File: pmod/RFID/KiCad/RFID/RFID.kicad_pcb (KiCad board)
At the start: 2 copper layers, 52.1 x 15.2 mm, 5 parts, among them J1 SPI IN, J3 SPI OUT

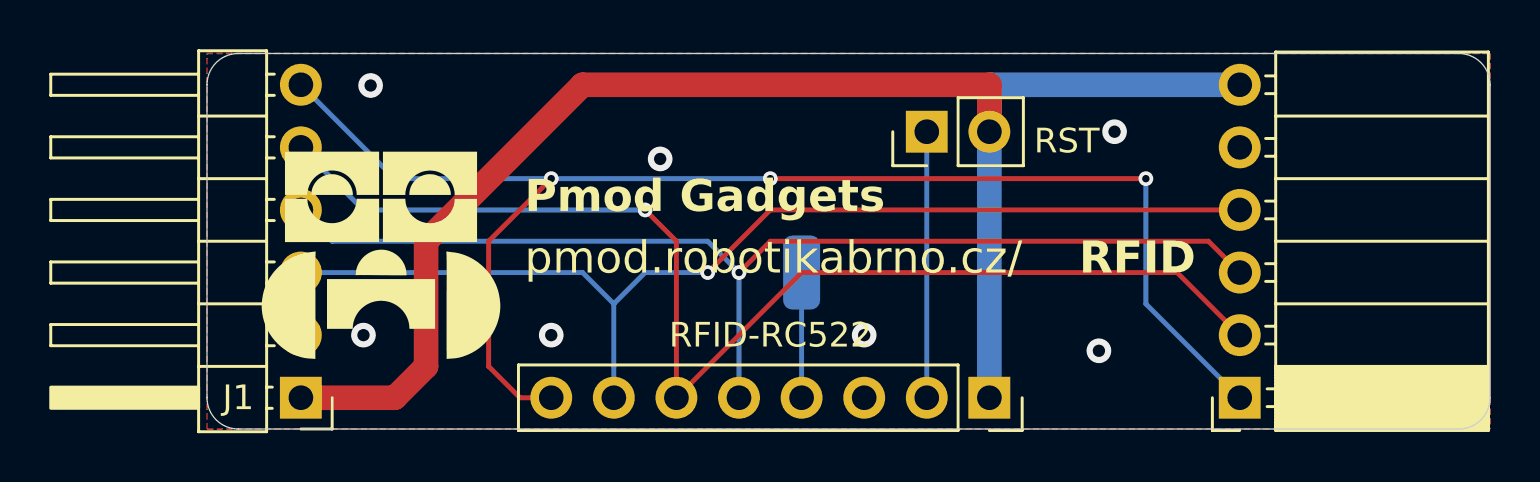
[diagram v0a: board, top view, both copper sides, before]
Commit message: Shrunk logos to not interfere with pins
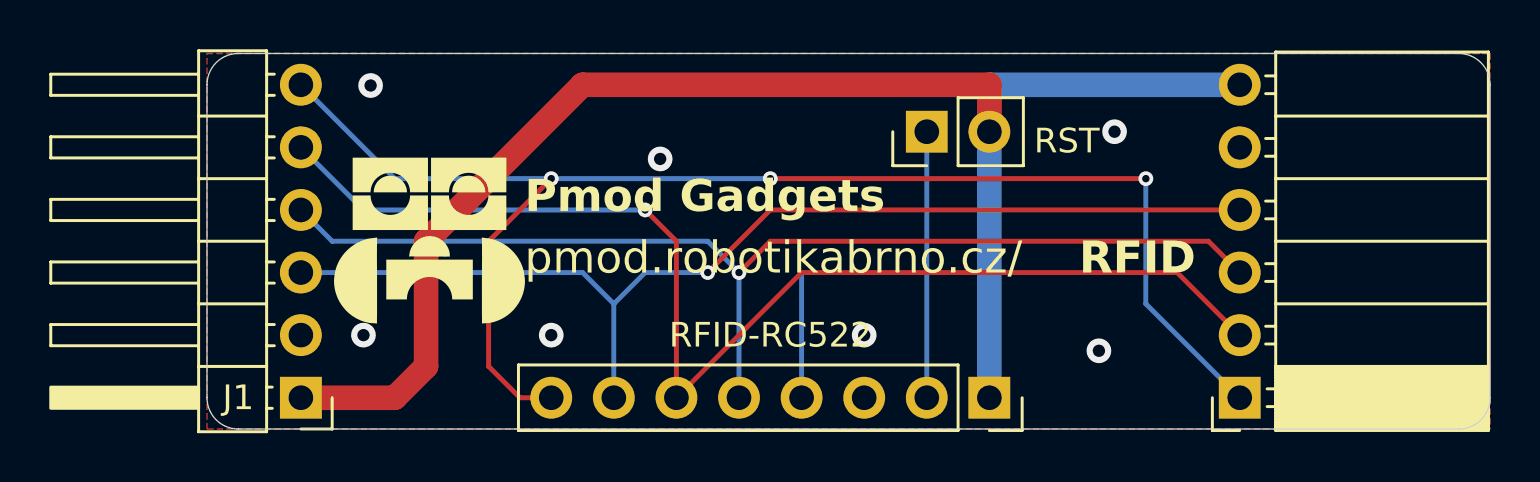
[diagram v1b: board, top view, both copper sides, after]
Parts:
- removed TP1: 1KQ, Connector_Wire:SolderWirePad_1x01_SMD_1.5x3mm

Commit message: minor fixes
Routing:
- net SS: track 58.1 -> 55.2 mm
- net GND: vias 7 -> 8
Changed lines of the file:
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@@
 			(psa4output no)
 			(plot_black_and_white yes)
+			(plotinvisibletext no)
 			(sketchpadsonfab no)
 			(plotpadnumbers no)
@@
 	)
 	(via
+		(at 65 58)
+		(size 0.6)
+		(drill 0.3)
+		(layers "F.Cu" "B.Cu")
+		(free yes)
+		(net 1)
+	)
+	(via
 		(at 91.44 47.625)
 		(size 1)
@@
 	)
 	(via
-		(at 68.58 55.88)
+		(at 70.2 55.88)
 		(size 1)
 		(drill 0.5)
@@
 	)
 	(via
-		(at 73 48.73)
+		(at 73.4 48)
 		(size 1)
 		(drill 0.5)
@@
 	)
 	(segment
-		(start 68.58 58.42)
-		(end 67.31 58.42)
-		(width 0.2)
-		(layer "F.Cu")
-		(net 5)
-	)
-	(segment
-		(start 67.31 58.42)
-		(end 66.04 57.15)
-		(width 0.2)
-		(layer "F.Cu")
-		(net 5)
-	)
-	(segment
-		(start 66.04 57.15)
-		(end 66.04 52.07)
-		(width 0.2)
-		(layer "F.Cu")
-		(net 5)
-	)
-	(segment
-		(start 66.04 52.07)
-		(end 68.58 49.53)
+		(start 68.58 49.53)
+		(end 68.58 58.42)
 		(width 0.2)
 		(layer "F.Cu")
@@
 		(priority 1)
 		(connect_pads
-			(clearance 0.5)
+			(clearance 0.25)
 		)
 		(min_thickness 0.25)
 		(filled_areas_thickness no)
 		(fill yes
-			(thermal_gap 0.5)
+			(thermal_gap 0.25)
 			(thermal_bridge_width 0.5)
 		)
@@
 		(hatch edge 0.5)
 		(connect_pads
-			(clearance 0.5)
+			(clearance 0.25)
 		)
 		(min_thickness 0.25)
 		(filled_areas_thickness no)
 		(fill yes
-			(thermal_gap 0.5)
+			(thermal_gap 0.25)
 			(thermal_bridge_width 0.5)
 		)

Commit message: fix: small pcb fixes
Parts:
- moved RFID-RC522 0.13 mm to (86.4, 58.3)
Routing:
- net Net-(J2-Pin_4): track 5.08 -> 0.00 mm
- net RST: track 11.4 -> 10.8 mm
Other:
- board size 52.1 x 15.2 mm -> 52.1 x 15.5 mm
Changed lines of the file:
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@@
 			(psa4output no)
 			(plot_black_and_white yes)
-			(plotinvisibletext no)
 			(sketchpadsonfab no)
 			(plotpadnumbers no)
@@
 	(footprint "Connector_PinSocket_2.54mm:PinSocket_1x08_P2.54mm_Vertical"
 		(layer "F.Cu")
-		(at 86.36 58.42 -90)
+		(at 86.36 58.293 -90)
 		(descr "Through hole straight socket strip, 1x08, 2.54mm pitch, single row (from Kicad 4.0.7), script generated")
 		(tags "Through hole socket strip THT 1x08 2.54mm single row")
@@
 	)
 	(gr_arc
-		(start 106.68 58.42)
-		(mid 106.308026 59.318026)
-		(end 105.41 59.69)
+		(start 106.68 58.547)
+		(mid 106.308026 59.445026)
+		(end 105.41 59.817)
 		(stroke
 			(width 0.05)
@@
 	)
 	(gr_line
-		(start 54.61 45.72)
-		(end 54.61 58.42)
+		(start 54.61 45.593)
+		(end 54.61 58.547)
 		(stroke
 			(width 0.05)
@@
 	)
 	(gr_arc
-		(start 54.61 45.72)
-		(mid 54.981974 44.821974)
-		(end 55.88 44.45)
+		(start 54.61 45.593)
+		(mid 54.981974 44.694974)
+		(end 55.88 44.323)
 		(stroke
 			(width 0.05)
@@
 	)
 	(gr_line
-		(start 106.68 58.42)
-		(end 106.68 45.72)
+		(start 106.68 58.547)
+		(end 106.68 45.593)
 		(stroke
 			(width 0.05)
@@
 	)
 	(gr_line
-		(start 55.88 59.69)
-		(end 105.41 59.69)
+		(start 55.88 59.817)
+		(end 105.41 59.817)
 		(stroke
 			(width 0.05)
@@
 	)
 	(gr_arc
-		(start 55.88 59.69)
-		(mid 54.981974 59.318026)
-		(end 54.61 58.42)
+		(start 55.88 59.817)
+		(mid 54.981974 59.445026)
+		(end 54.61 58.547)
 		(stroke
 			(width 0.05)
@@
 	)
 	(gr_arc
-		(start 105.41 44.45)
-		(mid 106.308026 44.821974)
-		(end 106.68 45.72)
+		(start 105.41 44.323)
+		(mid 106.308026 44.694974)
+		(end 106.68 45.593)
 		(stroke
 			(width 0.05)
@@
 	)
 	(gr_line
-		(start 105.41 44.45)
-		(end 55.88 44.45)
+		(start 105.41 44.323)
+		(end 55.88 44.323)
 		(stroke
 			(width 0.05)
@@
 		(start 95.25 52.07)
 		(end 77.47 52.07)
-		(width 0.2)
+		(width 0.3)
 		(layer "F.Cu")
 		(net 3)
@@
 		(start 77.47 52.07)
 		(end 76.2 53.34)
-		(width 0.2)
+		(width 0.3)
 		(layer "F.Cu")
 		(net 3)
@@
 		(start 96.52 53.34)
 		(end 95.25 52.07)
-		(width 0.2)
+		(width 0.3)
 		(layer "F.Cu")
 		(net 3)
@@
 		(start 74.93 52.07)
 		(end 76.2 53.34)
-		(width 0.2)
+		(width 0.3)
 		(layer "B.Cu")
 		(net 3)
@@
 		(start 58.42 50.8)
 		(end 59.69 52.07)
-		(width 0.2)
+		(width 0.3)
 		(layer "B.Cu")
 		(net 3)
@@
 		(start 59.69 52.07)
 		(end 74.93 52.07)
-		(width 0.2)
+		(width 0.3)
 		(layer "B.Cu")
 		(net 3)
@@
 		(start 76.2 53.34)
 		(end 76.2 58.42)
-		(width 0.2)
+		(width 0.3)
 		(layer "B.Cu")
 		(net 3)
@@
 		(start 77.47 50.8)
 		(end 96.52 50.8)
-		(width 0.2)
+		(width 0.3)
 		(layer "F.Cu")
 		(net 4)
@@
 		(start 74.93 53.34)
 		(end 77.47 50.8)
-		(width 0.2)
+		(width 0.3)
 		(layer "F.Cu")
 		(net 4)
@@
 		(start 74.93 53.34)
 		(end 72.39 53.34)
-		(width 0.2)
-		(layer "B.Cu")
-		(net 4)
-	)
-	(segment
-		(start 72.39 53.34)
-		(end 71.12 54.61)
-		(width 0.2)
+		(width 0.3)
 		(layer "B.Cu")
 		(net 4)
@@
 	(segment
 		(start 71.12 54.61)
-		(end 71.12 57.15)
-		(width 0.2)
+		(end 71.12 58.293)
+		(width 0.3)
 		(layer "B.Cu")
 		(net 4)
 	)
 	(segment
-		(start 71.12 57.15)
-		(end 71.12 58.42)
-		(width 0.2)
+		(start 72.39 53.34)
+		(end 71.12 54.61)
+		(width 0.3)
 		(layer "B.Cu")
 		(net 4)
@@
 		(start 69.85 53.34)
 		(end 71.12 54.61)
-		(width 0.2)
+		(width 0.3)
 		(layer "B.Cu")
 		(net 4)
@@
 		(start 58.42 53.34)
 		(end 69.85 53.34)
-		(width 0.2)
+		(width 0.3)
 		(layer "B.Cu")
 		(net 4)
@@
 		(start 68.58 49.53)
 		(end 68.58 58.42)
-		(width 0.2)
+		(width 0.3)
 		(layer "F.Cu")
 		(net 5)
@@
 		(start 77.47 49.53)
 		(end 92.71 49.53)
-		(width 0.2)
+		(width 0.3)
 		(layer "F.Cu")
 		(net 5)
@@
 		(start 68.58 49.53)
 		(end 77.47 49.53)
-		(width 0.2)
+		(width 0.3)
 		(layer "B.Cu")
 		(net 5)
@@
 		(start 68.58 49.53)
 		(end 62.23 49.53)
-		(width 0.2)
+		(width 0.3)
 		(layer "B.Cu")
 		(net 5)
@@
 		(start 92.71 54.61)
 		(end 96.52 58.42)
-		(width 0.2)
+		(width 0.3)
 		(layer "B.Cu")
 		(net 5)
@@
 		(start 92.71 49.53)
 		(end 92.71 54.61)
-		(width 0.2)
+		(width 0.3)
 		(layer "B.Cu")
 		(net 5)
@@
 		(start 62.23 49.53)
 		(end 58.42 45.72)
-		(width 0.2)
+		(width 0.3)
 		(layer "B.Cu")
 		(net 5)
 	)
 	(segment
-		(start 78.74 58.42)
-		(end 78.74 53.34)
-		(width 0.2)
-		(layer "B.Cu")
-		(net 6)
-	)
-	(segment
 		(start 83.82 58.42)
-		(end 83.82 46.99)
-		(width 0.2)
+		(end 83.82 47.625)
+		(width 0.3)
 		(layer "B.Cu")
 		(net 7)
@@
 		(start 72.39 50.8)
 		(end 73.66 52.07)
-		(width 0.2)
+		(width 0.3)
 		(layer "F.Cu")
 		(net 8)
@@
 		(start 78.74 53.34)
 		(end 93.98 53.34)
-		(width 0.2)
+		(width 0.3)
 		(layer "F.Cu")
 		(net 8)
@@
 		(start 93.98 53.34)
 		(end 96.52 55.88)
-		(width 0.2)
+		(width 0.3)
 		(layer "F.Cu")
 		(net 8)
@@
 		(start 73.66 52.07)
 		(end 73.66 58.42)
-		(width 0.2)
+		(width 0.3)
 		(layer "F.Cu")
 		(net 8)
@@
 		(start 73.66 58.42)
 		(end 78.74 53.34)
-		(width 0.2)
+		(width 0.3)
 		(layer "F.Cu")
 		(net 8)
@@
 		(start 60.96 50.8)
 		(end 58.42 48.26)
-		(width 0.2)
+		(width 0.3)
 		(layer "B.Cu")
 		(net 8)
@@
 		(start 72.39 50.8)
 		(end 60.96 50.8)
-		(width 0.2)
+		(width 0.3)
 		(layer "B.Cu")
 		(net 8)
@@
 		(polygon
 			(pts
-				(xy 54.61 44.45) (xy 106.68 44.45) (xy 106.68 59.69) (xy 54.61 59.69)
+				(xy 54.61 44.323) (xy 106.68 44.323) (xy 106.68 59.817) (xy 54.61 59.817)
 			)
 		)
@@
 		(polygon
 			(pts
-				(xy 106.68 44.45) (xy 106.68 59.69) (xy 54.61 59.69) (xy 54.61 44.45) (xy 63.5 44.45)
+				(xy 106.68 44.323) (xy 106.68 59.817) (xy 54.61 59.817) (xy 54.61 44.323) (xy 63.5 44.45)
 			)
 		)
